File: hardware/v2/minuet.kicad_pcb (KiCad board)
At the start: 2 copper layers, 79 x 79 mm, 127 parts, among them J101 B2P-VH-B, J102 B2B-XH-A_1, J103 PPPC062LFBN-RC, J104 B2B-XH-A_1, J201 USB4105-GF-A, J202 SM04B-SRSS-TB, J301 B3B-XH-A, J301 B3P-VH-B, J302 B5B-XH-A, J401 B2B-XH-A, J501 G800LE300018YEU, J502 MTJ-889X1, J503 MTJ-669X1, Q101 MMBT3904, SW201 EVQ-P7A01P, SW202 EVQ-P7A01P, U101 TSOP39238, U102 LMV331X-SC5R, U201 TCA9554PWR, U201 TCA9555RTWR, U202 ESP32-C3-WROOM-02, U301 DRV10970PWP, U301 MCT8315Z0HRRYR, U401 DRV8876PWPR

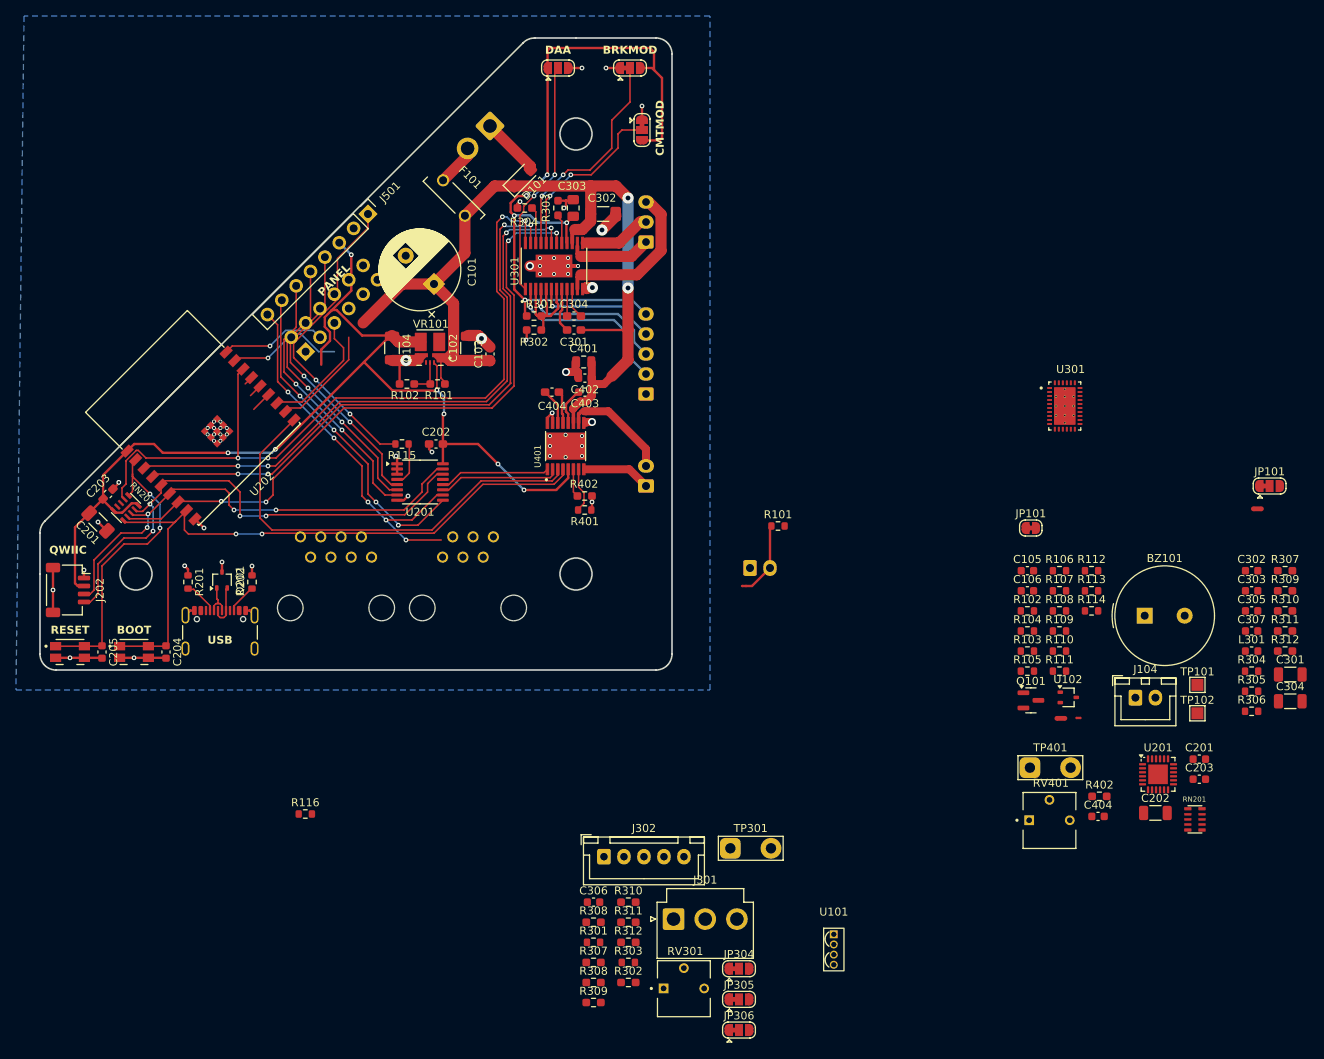
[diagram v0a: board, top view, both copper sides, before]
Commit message: Complete draft of the v2 PCB
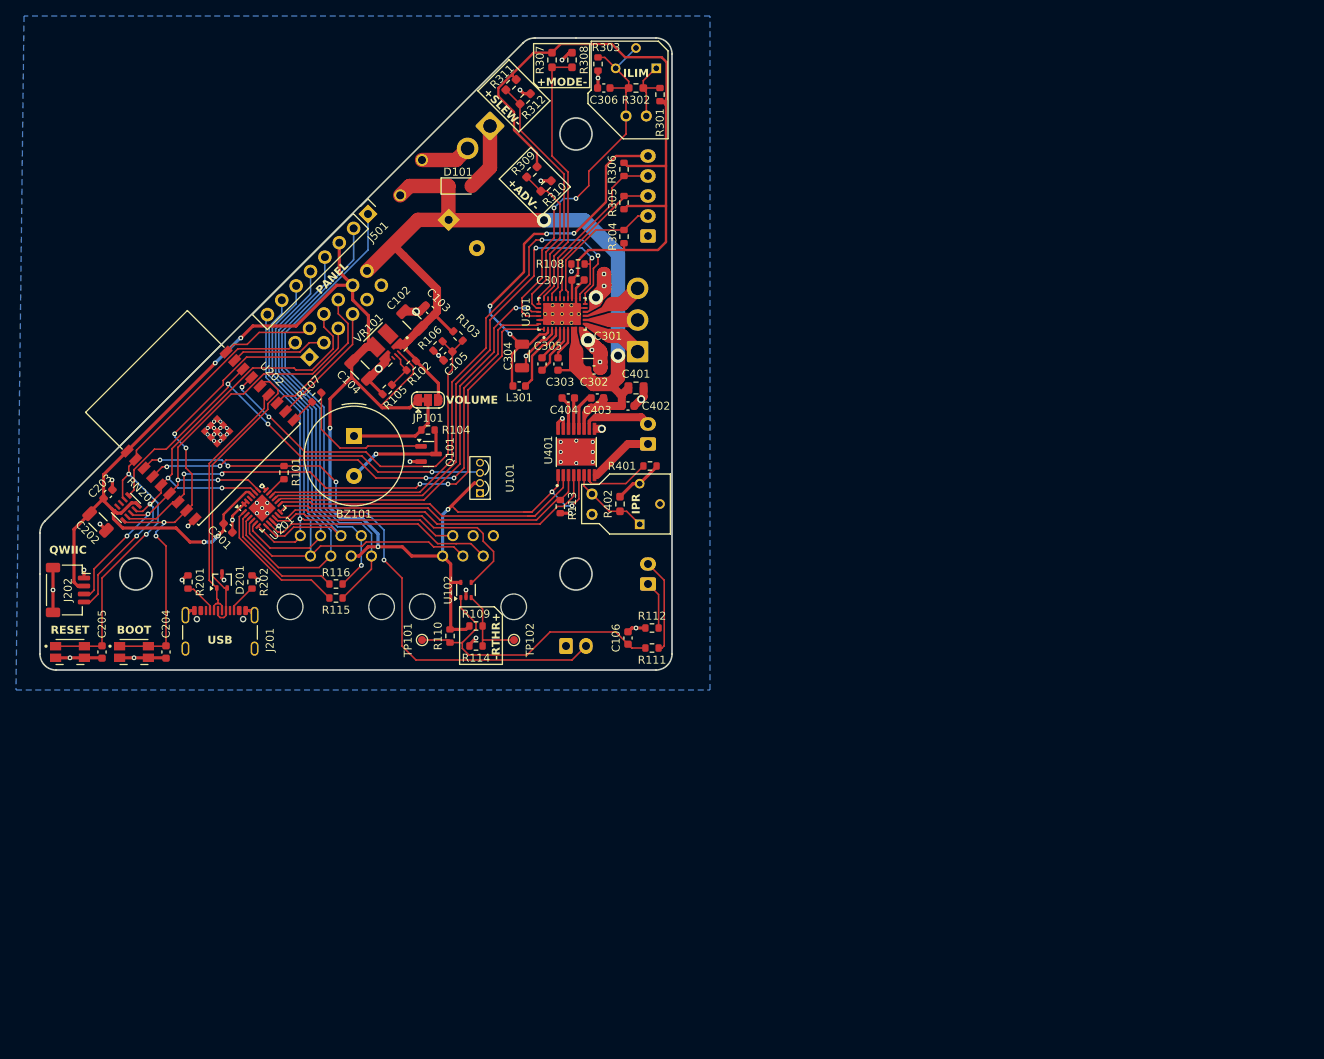
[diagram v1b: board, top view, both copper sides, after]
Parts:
- removed the C201 at (40.2, 93.5)
- removed the C202 at (82.5, 83.8)
- removed the C203 at (41.5, 90.0)
- removed the C301 at (99.8, 69.5)
- removed the C302 at (103.4, 55.0)
- removed the C303 at (99.7, 54.2)
- removed the C304 at (99.8, 67.8)
- removed the C404 at (97.0, 77.3)
- removed the J301 at (108.8, 58.5)
- removed the J302 at (108.8, 77.5)
- removed the JP101 at (156.8, 94.2)
- removed JP301, JP303, JP304, JP305, JP306: SolderJumper_3_Bridged12, Jumper:SolderJumper-3_P1.3mm_Bridged12_RoundedPad1.0x1.5mm
- removed JP302: SolderJumper_3_Open, Jumper:SolderJumper-3_P1.3mm_Open_RoundedPad1.0x1.5mm
- removed the NT101 at (121.0, 101.5)
- removed NT103: NetTie_2, Generic:NetTie-2_SMD_Pad0.6mm
- removed the R101 at (82.7, 76.2)
- removed the R102 at (78.9, 76.2)
- removed the R301 at (94.8, 67.8)
- removed the R302 at (94.8, 69.5)
- removed the R303 at (97.8, 54.2)
- removed the R304 at (93.6, 54.2)
- removed the R307 at (102.2, 148.5)
- removed the R308 at (102.2, 151.1)
- removed the R309 at (102.2, 153.6)
- removed the R310 at (106.5, 141.0)
- removed the R311 at (106.5, 143.5)
- removed the R312 at (106.5, 146.0)
- removed the R402 at (101.1, 90.2)
- removed the RN201 at (43.8, 91.8)
- removed the U201 at (80.5, 88.5)
- removed the U301 at (97.2, 61.5)
- added NT402: NetTie_2, Generic:NetTie-2_SMD_Pad0.2mm, F.Cu at (84.7, 91.7)
- C101: value 680u -> 1000u; moved to B.Cu
- F101, J301, J302, RV301, RV401: moved to B.Cu
- J102: value B2B-XH-A_1 -> B2B-XH-A
- J104: value B2B-XH-A_1 -> B2B-XH-A; moved to B.Cu
- NT101: footprint Generic:NetTie-2_SMD_Pad0.6mm -> Generic:NetTie-2_SMD_Pad1.0mm
- NT102: footprint Generic:NetTie-2_SMD_Pad0.3mm -> Generic:NetTie-2_SMD_Pad0.2mm
- TP101, TP102: footprint TestPoint:TestPoint_Pad_1.5x1.5mm -> TestPoint:TestPoint_Pad_D1.0mm
- TP301, TP401: footprint TestPoint:TestPoint_2Pads_Pitch5.08mm_Drill1.3mm -> TestPoint:TestPoint_2Pads_Pitch2.54mm_Drill0.8mm; moved to B.Cu
- U102: footprint Package_TO_SOT_SMD:SOT-323_SC-70 -> Package_TO_SOT_SMD:SOT-353_SC-70-5
- moved C203 141.0 mm to (41.5, 90.0), turned to 45 degrees
- moved RN201 139.2 mm to (43.8, 91.8), turned to 135 degrees
- moved C202 137.1 mm to (40.2, 93.5), turned to 135 degrees
- moved C201 124.8 mm to (56.5, 94.2), turned to -45 degrees
- moved R311 118.4 mm to (91.9, 38.8), turned to -135 degrees
- moved R312 117.4 mm to (93.6, 40.6), turned to 45 degrees
- moved U201 116.8 mm to (60.8, 91.8), turned to 45 degrees
- moved RV301 115.2 mm to (107.5, 36.8), turned to 180 degrees
- moved R303 112.4 mm to (102.8, 36.2), turned to -90 degrees
- moved R302 111.8 mm to (107.5, 39.2), turned to 180 degrees
- moved R307 111.7 mm to (97.0, 35.8), turned to -90 degrees
- moved R308 107.8 mm to (99.5, 35.8), turned to 90 degrees
- moved R309 107.7 mm to (94.5, 49.7), turned to -135 degrees
- moved R310 106.6 mm to (96.2, 51.5), turned to 45 degrees
- moved R301 106.3 mm to (110.5, 40.1), turned to 90 degrees
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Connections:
- net Net-(U102--) renamed /RTHR
- C102 pad 1: Net-(VR101-VIN) -> /12V_PWR
- C103 pad 1: Net-(VR101-VIN) -> /12V_PWR
- C105 pad 1: GPIO4 -> GPIO3
- J102 pad 2: GPIO3 -> GPIO4
- J103 pad 1: GND -> BOOT
- J103 pad 10: BOOT -> +3.3V
- J103 pad 2: +3.3V -> RESET
- J103 pad 3: GPIO0 -> GPIO1
- J103 pad 4: GPIO1 -> GPIO0
- J103 pad 5: UART_TXD -> SDA
- J103 pad 6: UART_RXD -> SCL
- J103 pad 7: SCL -> UART_RXD
- J103 pad 8: SDA -> UART_TXD
- J103 pad 9: RESET -> GND
- J501 pad 4: XIO5 -> XIO6
- J501 pad 5: XIO4 -> XIO2
- J501 pad 6: XIO3 -> XIO4
- J501 pad 7: XIO1 -> XIO3
- J501 pad 8: XIO0 -> XIO5
- J502 pad 4: XIO5 -> XIO6
- J502 pad 5: XIO4 -> XIO2
- J502 pad 6: XIO3 -> XIO4
- J502 pad 7: XIO1 -> XIO3
- J502 pad 8: XIO0 -> XIO5
- J503 pad 2: XIO2 -> XIO7
- J503 pad 4: XIO1 -> XIO3
- J503 pad 5: XIO0 -> XIO5
- JP101 pad 3: Net-(JP101-B) -> /12V_PWR
- NT101 pad 2: Net-(VR101-VIN) -> /12V_PWR
- NT102 pad 1: +12V -> Net-(VR101-VOS)
- NT102 pad 2: Net-(NT102-Pad2) -> +3.3V
- R101 pad 1: GPIO3 -> GPIO4
- R101 pad 2: XIO14 -> XIO15
- R102 pad 1: Net-(VR101-VIN) -> /12V_PWR
- R103 pad 1: GPIO4 -> GPIO3
- R103 pad 2: Net-(NT102-Pad2) -> /12V_PWR
- R106 pad 2: GPIO4 -> GPIO3
- R108 pad 2: XIO8 -> XIO13
- R113 pad 2: XIO11 -> XIO10
- R115 pad 1: XIO7 -> XIO0
- R116 pad 1: XIO6 -> XIO1
- RN201 pad 6: RESET -> GPIO2_STRAP
- RN201 pad 7: GPIO2_STRAP -> RESET
- U301 pad 16: XIO10 -> XIO14
- U301 pad 17: XIO8 -> XIO13
- U301 pad 29: XIO9 -> XIO12
- U301 pad 34: (no net) -> GND
- U301 pad 35: (no net) -> GND
- U301 pad 36: (no net) -> GND
- U301 pad 37: (no net) -> GND
- U301 pad 38: (no net) -> GND
- U301 pad 39: (no net) -> GND
- U301 pad 40: (no net) -> GND
- U301 pad 41: (no net) -> GND
- U301 pad 42: (no net) -> GND
- U301 pad 43: (no net) -> GND
- U301 pad 44: (no net) -> GND
- U401 pad 1: +3.3V -> /cover/VREF
- U401 pad 2: XIO12 -> XIO11
- U401 pad 3: XIO11 -> XIO10
- U401 pad 4: XIO13 -> XIO9
- U401 pad 5: +3.3V -> /cover/VREF
- VR101 pad 1: Net-(VR101-VIN) -> /12V_PWR
- VR101 pad 7: +3.3V -> Net-(VR101-VOS)
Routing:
- net IO2_STRAP: track 95.6 -> 0.00 mm, vias 4 -> 0
- net /fan/VINT: track 92.1 -> 0.00 mm, vias 5 -> 0
- net /fan/AVDD: track 0.00 -> 90.0 mm
- net IO8_STRAP: track 82.8 -> 0.00 mm, vias 4 -> 0
- net IO5: track 76.2 -> 0.00 mm, vias 4 -> 0
- net GPIO4: track 0.00 -> 75.8 mm, vias 0 -> 4
- net IO4: track 75.4 -> 0.00 mm, vias 4 -> 0
- net GPIO8_STRAP: track 0.00 -> 72.8 mm, vias 0 -> 4
- net XIO14: track 0.00 -> 71.5 mm, vias 0 -> 2
- net XIO13: track 0.00 -> 69.3 mm, vias 0 -> 2
- net GPIO5: track 0.00 -> 65.7 mm, vias 0 -> 4
- net GPIO2_STRAP: track 0.00 -> 58.5 mm, vias 0 -> 3
- net (no net): track 55.4 -> 0.00 mm
- net /keypad/LED_RAIN: track 0.00 -> 54.3 mm, vias 0 -> 1
- net XIO12: track 0.00 -> 50.4 mm, vias 0 -> 2
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- added copper zone on F.Cu, net GND
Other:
- board text added: "+ADV-"
- board text added: "+MODE-"
- board text added: "+SLEW-"
- board text added: "-RTHR+"
- board text added: "12V 3V3 TXD SCL GPIO0 RESET"
- board text added: "4 KEY WALL CONTROL"
- board text added: "6 KEY WALL CONTROL"
- board text added: "COVER CURRENT LIMIT"
- board text added: "COVER MOTOR"
- board text added: "ESP32-C3"
- board text added: "FAN CURRENT LIMIT"
- board text added: "GND GND RXD SDA GPIO1 BOOT"
- board text added: "ILIM"
- board text added: "IPR"
- board text added: "RAIN"
- board text added: "TEMP"
- board text added: "VOLUME"
- board text added: "github.com/j9brown/minuet Brown Studios Minuet Fan Controller 2024/2, v2.0"
- board text removed: "12V RX IO1 3V3"
- board text removed: "BRKMOD"
- board text removed: "Brown Studios Minuet Fan Controller 2024/12/9, v1.1"
- board text removed: "CMTMOD"
- board text removed: "DAA"
- board text removed: "GND TX IO0 GND"
- board text removed: "THERMISTOR"
- board text removed: "cover MOTOR"

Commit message: Prepare Minuet v2 for fabrication.
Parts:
- R109: value 22K -> 100K
- R114: value 100K -> 1.5M
- moved C101 5.12 mm to (89.2, 55.8), turned to -90 degrees
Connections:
- net Net-(U102-+) renamed /RSEN
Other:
- board text added: "EXPANSION BOARD"
